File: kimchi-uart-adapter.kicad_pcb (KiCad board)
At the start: 2 copper layers, 50 x 20 mm, 29 parts, among them IC1 MIC5504-1.8YM5-TR, J1 TYPE-C-31-M-12, J2 Conn_01x02, J3 SM06B-SRSS-TB(LF)(SN), U1 TPD2E001DRSR, U2 FT230XS

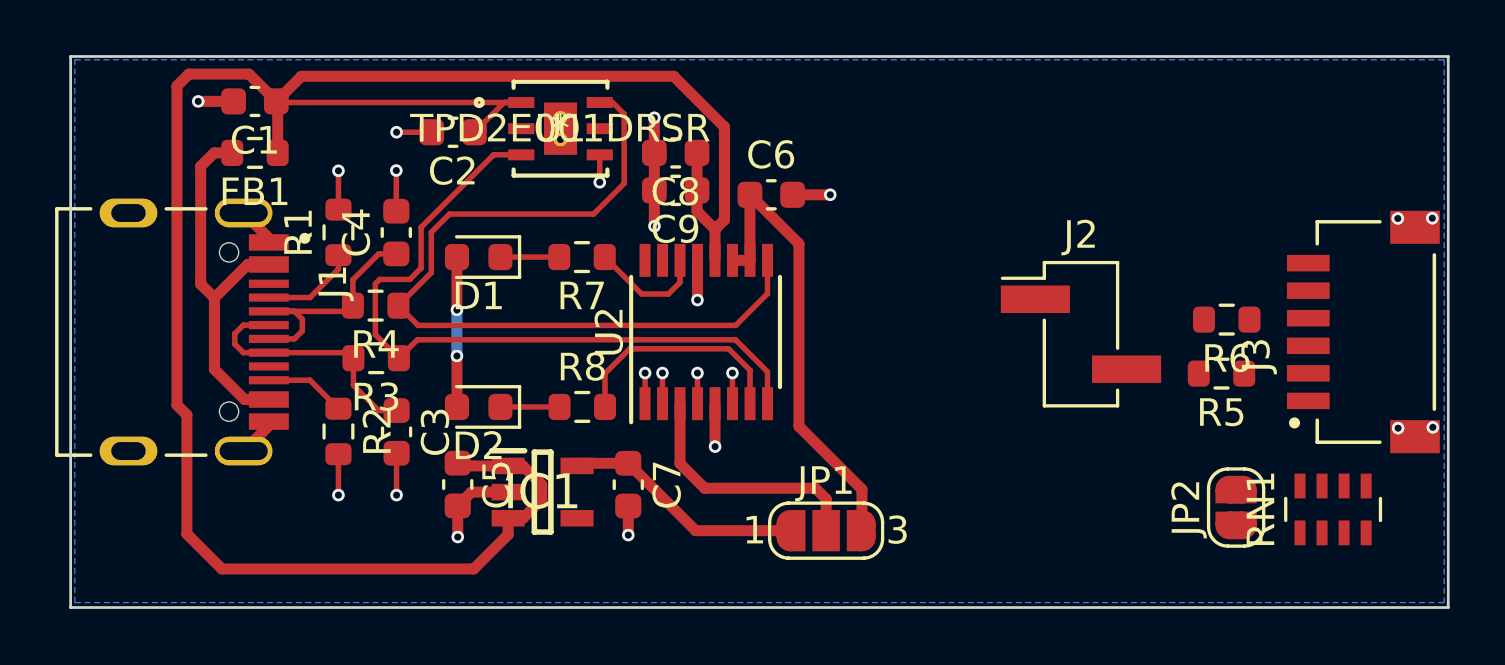
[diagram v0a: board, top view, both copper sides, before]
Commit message: Almost completed routing, waiting for fix to the resistor network issue. Also replaced model for TPD2E001 chip
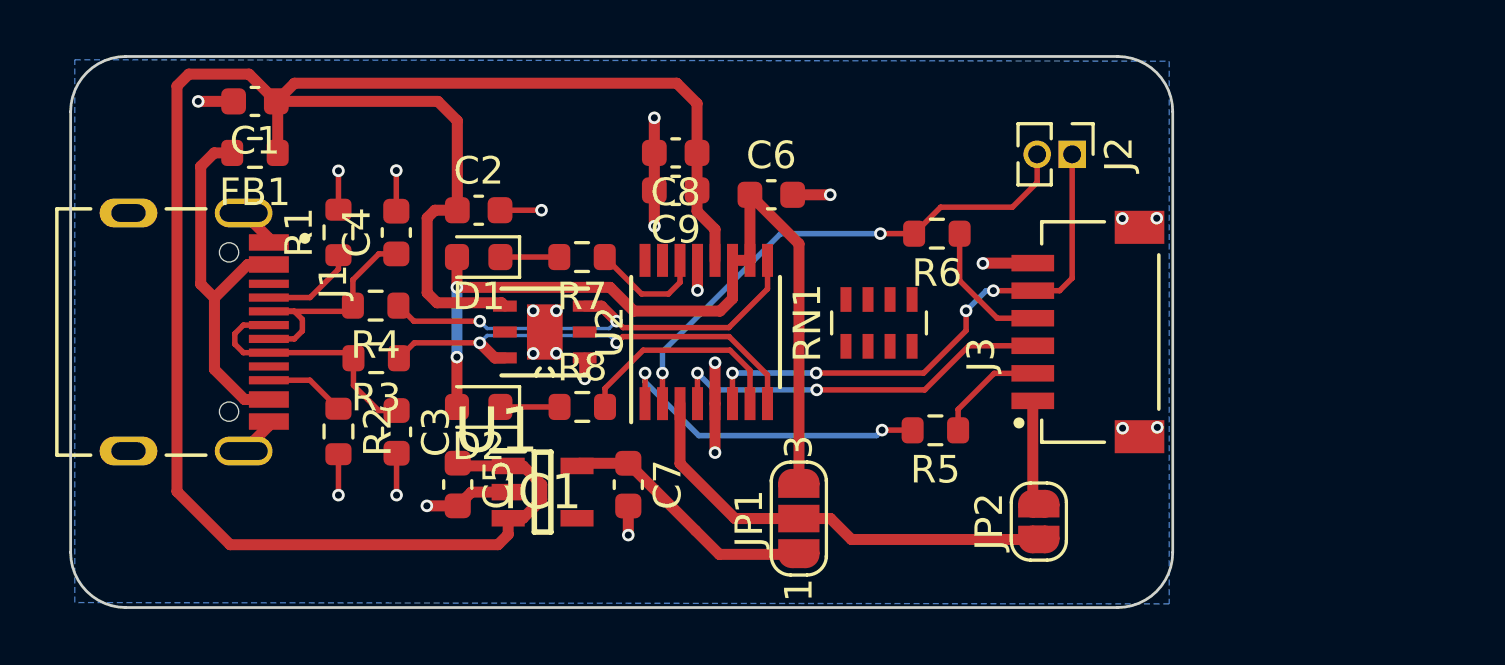
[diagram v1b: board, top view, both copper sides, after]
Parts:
- J2: footprint Connector_PinHeader_2.54mm:PinHeader_1x02_P2.54mm_Vertical_SMD_Pin1Left -> Connector_PinHeader_1.27mm:PinHeader_1x02_P1.27mm_Vertical
- U1: footprint footprints:TPD2E001DRSR -> footprints:SON95P315X315X80-7N
- moved RN1 17.8 mm to (163.2, 100.0)
- moved R6 11.0 mm to (165.3, 96.8)
- moved R5 10.6 mm to (165.2, 103.9)
- moved J3 10.0 mm to (168.8, 100.4)
- moved U1 7.40 mm to (151.1, 100.4), turned to 180 degrees
- moved JP2 7.18 mm to (169.0, 107.3)
- moved J2 6.54 mm to (170.2, 93.9), turned to 270 degrees
- moved C2 2.98 mm to (148.7, 96.0), turned to 0 degrees
- moved JP1 1.08 mm to (160.3, 107.2), turned to 90 degrees
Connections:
- D1 pad 2: +1V8 -> +3V3
- D2 pad 2: +1V8 -> +3V3
- U1 pad 1: VBUS -> GND
- U1 pad 3: /D1+ -> /D1-
- U1 pad 4: GND -> VBUS
- U1 pad 6: /D1- -> /D1+
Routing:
- net /CTS: track 1.11 -> 19.8 mm, vias 1 -> 4
- net /RTS: track 1.11 -> 19.0 mm, vias 1 -> 2
- net +3V3: track 16.9 -> 31.6 mm, vias 0 -> 2
- net /RX: track 1.11 -> 14.2 mm, vias 1 -> 2
- net /D1-: track 29.8 -> 17.5 mm, vias 0 -> 2
- net /TX: track 1.11 -> 12.0 mm, vias 1 -> 2
- net /D1+: track 26.4 -> 16.7 mm, vias 0 -> 2
- net /VCCIO: track 9.16 -> 16.3 mm
- net Net-(J3-Pad4): track 0.00 -> 4.92 mm
- net +1V8: track 14.2 -> 9.46 mm, vias 2 -> 0
- net Net-(J3-Pad2): track 0.00 -> 4.01 mm
- net /VCC_KIMCHI: track 0.00 -> 3.82 mm
- net GND: track 24.9 -> 28.0 mm, vias 18 -> 24
- net VBUS: track 77.7 -> 78.7 mm
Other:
- board size 50 x 20 mm -> 40 x 20 mm

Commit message: Completed routing
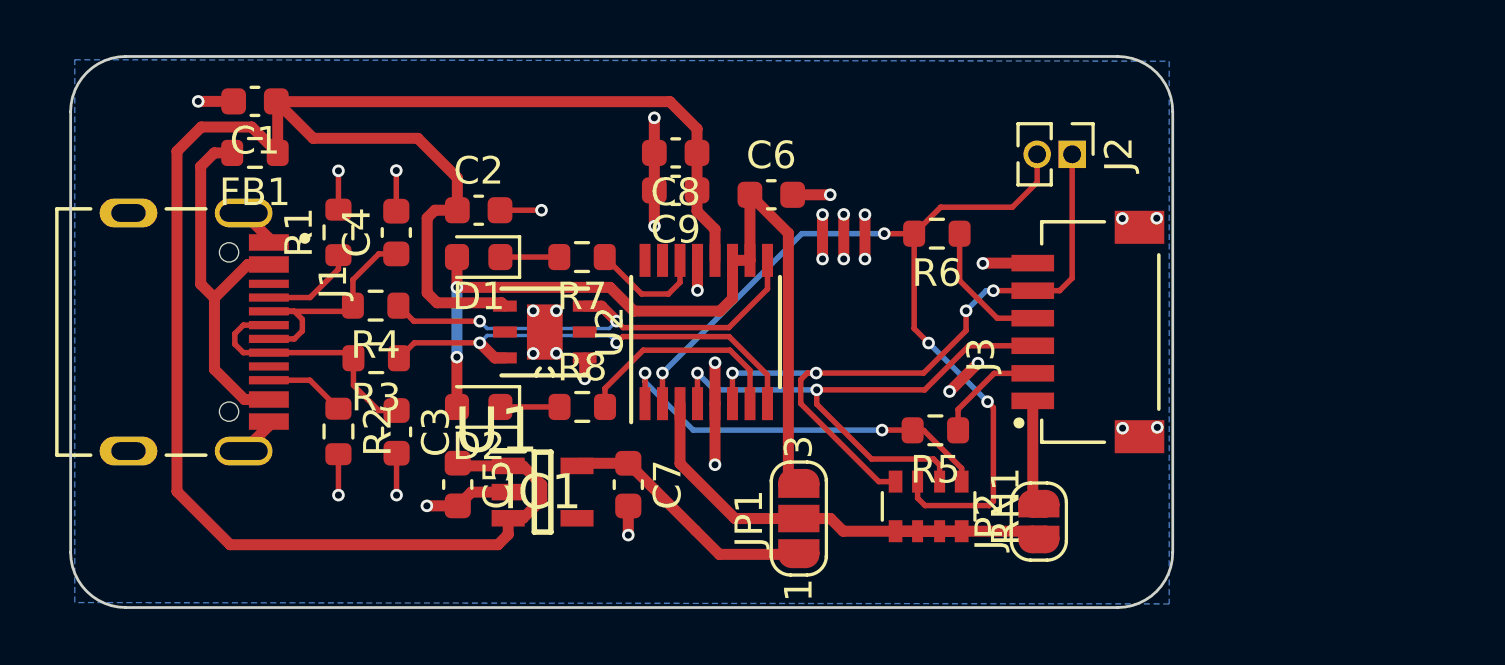
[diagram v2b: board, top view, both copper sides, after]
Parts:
- RN1: value R_Network04_US -> 10k; footprint Resistor_SMD:R_Array_Concave_4x0603 -> Resistor_SMD:R_Array_Convex_4x0603
- moved RN1 6.90 mm to (165.0, 106.7), turned to 270 degrees
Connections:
- RN1 pad 1: /VCCIO -> /TX
- RN1 pad 2: /TX -> /RX
- RN1 pad 3: /RX -> /RTS
- RN1 pad 4: /RTS -> /CTS
- RN1 pad 5: /CTS -> /VCCIO
- RN1 pad 6: (no net) -> /VCCIO
- RN1 pad 7: (no net) -> /VCCIO
- RN1 pad 8: (no net) -> /VCCIO
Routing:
- net /RTS: track 19.0 -> 33.0 mm, vias 2 -> 4
- net GND: track 28.0 -> 34.8 mm, vias 24 -> 32
- net /RX: track 14.2 -> 20.7 mm
- net /CTS: track 19.8 -> 25.9 mm
- net VBUS: track 78.7 -> 74.3 mm
- net /TX: track 12.0 -> 14.7 mm
- net /VCCIO: track 16.3 -> 18.7 mm
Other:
- rule trace_min: 0.0762 -> 0.127

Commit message: Completed routing of uart lid
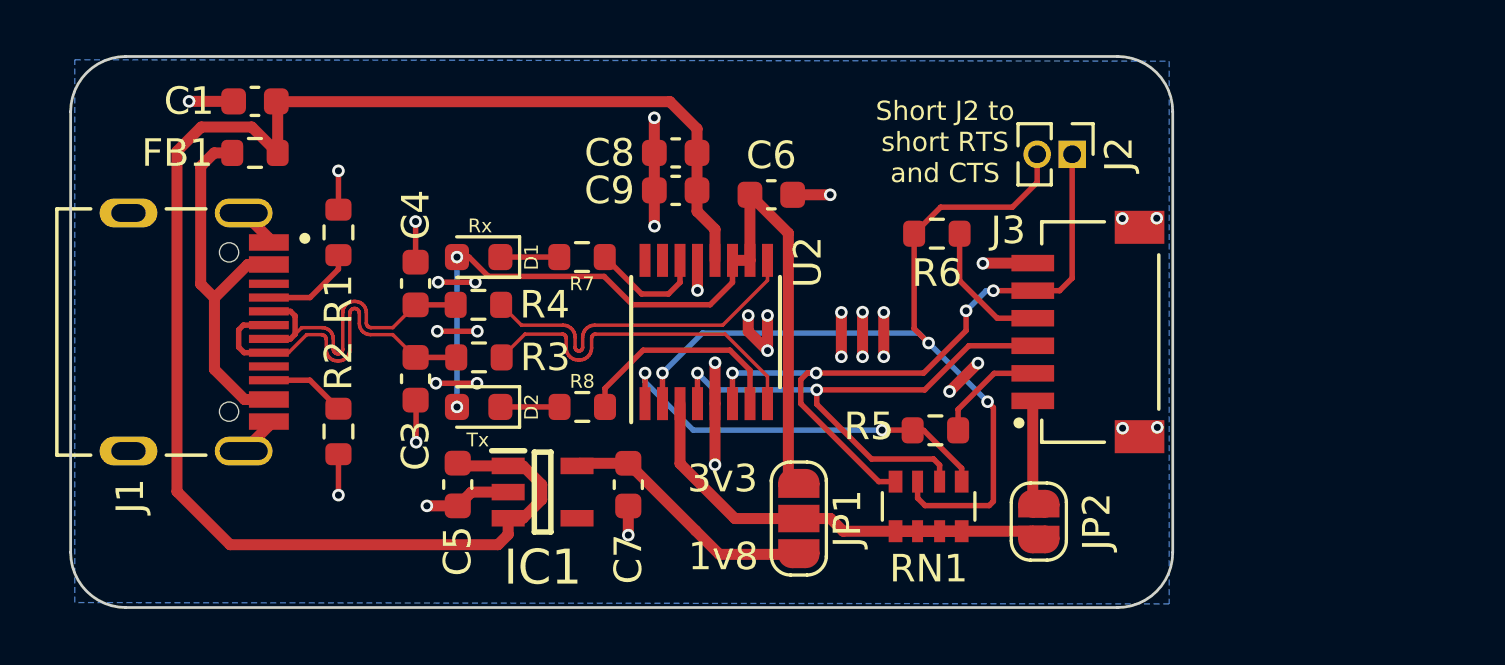
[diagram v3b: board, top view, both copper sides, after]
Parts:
- removed C2: 0.1uF, Capacitor_SMD:C_0603_1608Metric
- removed U1: TPD2E001DRSR, footprints:SON95P315X315X80-7N
- added REF**: OSHW-Logo2_7.3x6mm_SilkScreen, Symbol:OSHW-Logo2_7.3x6mm_SilkScreen, B.Cu at (138.9, 100.2)
- moved R4 3.73 mm to (148.7, 99.4)
- moved R3 3.73 mm to (148.7, 101.3)
- moved C3 2.05 mm to (146.4, 102.1)
- moved C4 1.98 mm to (146.4, 98.6)
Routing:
- net VBUS: track 74.3 -> 58.4 mm
- net GND: track 34.8 -> 40.0 mm, vias 32 -> 35
- net /D1-: track 17.5 -> 12.8 mm, vias 2 -> 0
- net /D+: track 9.19 -> 13.5 mm
- net /D-: track 9.13 -> 13.1 mm
- net /D1+: track 16.7 -> 13.0 mm, vias 2 -> 0
- net /RTS: track 33.0 -> 32.2 mm, vias 4 -> 3
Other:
- board text added: "1v8"
- board text added: "3v3"
- board text added: "Designed by Vedant Paranjape ve0x10.in"
- board text added: "Rx"
- board text added: "Short J2 to short RTS and CTS"
- board text added: "Tx"
- board text added: "USB to UART lid kimchi-micro"

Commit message: Updated silkscreen text
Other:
- board text added: "USB to UART adapter kimchi-micro"
- board text removed: "USB to UART lid kimchi-micro"

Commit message: Fixed changes requested during review, added gerbers and render images
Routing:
- net GND: track 40.0 -> 35.7 mm, vias 35 -> 29
- net +3V3: track 31.5 -> 31.0 mm, vias 2 -> 0
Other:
- rule pad_to_mask_clearance: 0.0508 -> 0
- rule trace_min: 0.127 -> 0.0762
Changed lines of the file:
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@@
-(kicad_pcb (version 20171130) (host pcbnew 5.1.10-88a1d61d58~88~ubuntu20.04.1)
+(kicad_pcb (version 20171130) (host pcbnew 5.1.10-88a1d61d58~90~ubuntu20.04.1)
   (general
     (thickness 1.6)
     (drawings 17)
-    (tracks 428)
+    (tracks 415)
     (zones 0)
     (modules 28)
@@
     (zone_clearance 0.508)
     (zone_45_only no)
-    (trace_min 0.127)
+    (trace_min 0.0762)
     (via_size 0.4572)
     (via_drill 0.254)
@@
     (pad_size 0.508 0.508)
     (pad_drill 0.254)
-    (pad_to_mask_clearance 0.0508)
-    (solder_mask_min_width 0.1016)
+    (pad_to_mask_clearance 0)
     (aux_axis_origin 0 0)
     (visible_elements FFFFFF7F)
@@
       (outputformat 1)
       (mirror false)
-      (drillshape 1)
+      (drillshape 0)
       (scaleselection 1)
-      (outputdirectory ""))
+      (outputdirectory "gerbers/"))
   )
   (net 0 "")
@@
     )
   )
+  (dimension 20 (width 0.15) (layer Dwgs.User)
+    (gr_text "20.000 mm" (at 178.78504 100.38 270) (layer Dwgs.User)
+      (effects (font (size 1 1) (thickness 0.15)))
+    )
+    (feature1 (pts (xy 171.85 110.38) (xy 178.071461 110.38)))
+    (feature2 (pts (xy 171.85 90.38) (xy 178.071461 90.38)))
+    (crossbar (pts (xy 177.48504 90.38) (xy 177.48504 110.38)))
+    (arrow1a (pts (xy 177.48504 110.38) (xy 176.898619 109.253496)))
+    (arrow1b (pts (xy 177.48504 110.38) (xy 178.071461 109.253496)))
+    (arrow2a (pts (xy 177.48504 90.38) (xy 176.898619 91.506504)))
+    (arrow2b (pts (xy 177.48504 90.38) (xy 178.071461 91.506504)))
+  )
+  (dimension 40 (width 0.15) (layer Dwgs.User)
+    (gr_text "40.000 mm" (at 153.85 114.680519) (layer Dwgs.User)
+      (effects (font (size 1 1) (thickness 0.15)))
+    )
+    (feature1 (pts (xy 173.85 108.38) (xy 173.85 113.96694)))
+    (feature2 (pts (xy 133.85 108.38) (xy 133.85 113.96694)))
+    (crossbar (pts (xy 133.85 113.380519) (xy 173.85 113.380519)))
+    (arrow1a (pts (xy 173.85 113.380519) (xy 172.723496 113.96694)))
+    (arrow1b (pts (xy 173.85 113.380519) (xy 172.723496 112.794098)))
+    (arrow2a (pts (xy 133.85 113.380519) (xy 134.976504 113.96694)))
+    (arrow2b (pts (xy 133.85 113.380519) (xy 134.976504 112.794098)))
+  )
+  (gr_text "USB to UART\nadapter\n kimchi-micro" (at 146.09318 100.05314 90) (layer B.SilkS)
+    (effects (font (size 1.5 1.5) (thickness 0.3)) (justify mirror))
+  )
   (gr_text "Designed by\nVedant Paranjape\nve0x10.in" (at 153.70556 100.5078 90) (layer B.SilkS)
     (effects (font (size 1.2 1.2) (thickness 0.3)) (justify mirror))
   )
-  (gr_text "USB to UART\nadapter\n kimchi-micro" (at 146.09318 100.05314 90) (layer B.SilkS)
-    (effects (font (size 1.5 1.5) (thickness 0.3)) (justify mirror))
-  )
   (gr_text "Short J2 to \nshort RTS \nand CTS" (at 165.58768 93.48724) (layer F.SilkS)
     (effects (font (size 0.7 0.7) (thickness 0.175)))
@@
   (gr_text Rx (at 148.71192 96.53016) (layer F.SilkS)
     (effects (font (size 0.5 0.5) (thickness 0.125)))
-  )
-  (dimension 20.010002 (width 0.15) (layer Dwgs.User)
-    (gr_text "20.010 mm" (at 180.894353 100.360452 -89.97136643) (layer Dwgs.User)
-      (effects (font (size 1 1) (thickness 0.15)))
-    )
-    (feature1 (pts (xy 171.79 90.36) (xy 180.175774 90.355809)))
-    (feature2 (pts (xy 171.8 110.37) (xy 180.185774 110.365809)))
-    (crossbar (pts (xy 179.599353 110.366102) (xy 179.589353 90.356102)))
-    (arrow1a (pts (xy 179.589353 90.356102) (xy 180.176337 91.482313)))
-    (arrow1b (pts (xy 179.589353 90.356102) (xy 179.003495 91.482899)))
-    (arrow2a (pts (xy 179.599353 110.366102) (xy 180.185211 109.239305)))
-    (arrow2b (pts (xy 179.599353 110.366102) (xy 179.012369 109.239891)))
-  )
-  (dimension 40.02008 (width 0.15) (layer Dwgs.User)
-    (gr_text "40.020 mm" (at 153.767127 114.489756 359.8854659) (layer Dwgs.User)
-      (effects (font (size 1 1) (thickness 0.15)))
-    )
-    (feature1 (pts (xy 173.79 108.09) (xy 173.778553 113.816178)))
-    (feature2 (pts (xy 133.77 108.01) (xy 133.758553 113.736178)))
-    (crossbar (pts (xy 133.759726 113.149759) (xy 173.779726 113.229759)))
-    (arrow1a (pts (xy 173.779726 113.229759) (xy 172.652052 113.813927)))
-    (arrow1b (pts (xy 173.779726 113.229759) (xy 172.654397 112.641088)))
-    (arrow2a (pts (xy 133.759726 113.149759) (xy 134.885055 113.73843)))
-    (arrow2b (pts (xy 133.759726 113.149759) (xy 134.8874 112.565591)))
   )
   (gr_line (start 173.85 108.38) (end 173.85 92.38) (layer Edge.Cuts) (width 0.1))
@@
   (segment (start 146.38782 104.37782) (end 146.39 104.38) (width 0.2) (layer F.Cu) (net 2))
   (segment (start 146.38782 102.85252) (end 146.38782 104.37782) (width 0.2) (layer F.Cu) (net 2))
-  (via (at 147.15744 100.35286) (size 0.4572) (drill 0.254) (layers F.Cu B.Cu) (net 2))
-  (via (at 148.61286 100.35286) (size 0.4572) (drill 0.254) (layers F.Cu B.Cu) (net 2))
-  (segment (start 147.15744 100.35286) (end 148.61286 100.35286) (width 0.2) (layer F.Cu) (net 2))
-  (via (at 147.10664 102.24008) (size 0.4572) (drill 0.254) (layers F.Cu B.Cu) (net 2))
-  (via (at 148.60016 102.24008) (size 0.4572) (drill 0.254) (layers F.Cu B.Cu) (net 2))
-  (segment (start 147.10664 102.24008) (end 148.60016 102.24008) (width 0.2) (layer F.Cu) (net 2))
-  (via (at 147.19046 98.57232) (size 0.4572) (drill 0.254) (layers F.Cu B.Cu) (net 2))
-  (via (at 148.5392 98.57486) (size 0.4572) (drill 0.254) (layers F.Cu B.Cu) (net 2))
-  (segment (start 148.53666 98.57232) (end 148.5392 98.57486) (width 0.2) (layer F.Cu) (net 2))
-  (segment (start 147.19046 98.57232) (end 148.53666 98.57232) (width 0.2) (layer F.Cu) (net 2))
   (via (at 158.44266 99.7839) (size 0.4572) (drill 0.254) (layers F.Cu B.Cu) (net 2))
   (via (at 159.1437 99.78136) (size 0.4572) (drill 0.254) (layers F.Cu B.Cu) (net 2))
@@
   (segment (start 158.505 97.7775) (end 158.5075 97.78) (width 0.4) (layer F.Cu) (net 5))
   (segment (start 158.505 95.4) (end 158.505 97.7775) (width 0.4) (layer F.Cu) (net 5))
-  (segment (start 147.87 103.0975) (end 147.8725 103.1) (width 0.4) (layer F.Cu) (net 5))
   (segment (start 159.9 105.47) (end 160.28 105.85) (width 0.4) (layer F.Cu) (net 5))
   (segment (start 159.9 96.795) (end 159.9 105.47) (width 0.4) (layer F.Cu) (net 5))
   (segment (start 158.505 95.4) (end 159.9 96.795) (width 0.4) (layer F.Cu) (net 5))
-  (segment (start 147.87 97.6625) (end 147.8725 97.66) (width 0.4) (layer F.Cu) (net 5))
   (segment (start 147.8725 97.66) (end 147.8725 97.66) (width 0.4) (layer F.Cu) (net 5))
-  (via (at 147.8725 97.66) (size 0.4572) (drill 0.254) (layers F.Cu B.Cu) (net 5))
   (segment (start 147.8725 103.1) (end 147.8725 103.1) (width 0.4) (layer F.Cu) (net 5))
-  (via (at 147.8725 103.1) (size 0.4572) (drill 0.254) (layers F.Cu B.Cu) (net 5))
-  (segment (start 147.8725 97.66) (end 147.8725 103.1) (width 0.2) (layer B.Cu) (net 5))
-  (segment (start 149.01201 98.36201) (end 148.31 97.66) (width 0.2) (layer F.Cu) (net 5))
-  (segment (start 153.21334 98.36201) (end 149.01201 98.36201) (width 0.2) (layer F.Cu) (net 5))
-  (segment (start 148.31 97.66) (end 147.8725 97.66) (width 0.2) (layer F.Cu) (net 5))
-  (segment (start 154.241529 99.390199) (end 153.21334 98.36201) (width 0.2) (layer F.Cu) (net 5))
+  (segment (start 147.87 103.0975) (end 147.8725 103.1) (width 0.4) (layer F.Cu) (net 5))
+  (segment (start 157.062301 99.390199) (end 154.241529 99.390199) (width 0.2) (layer F.Cu) (net 5))
+  (segment (start 157.8725 97.78) (end 157.8725 98.58) (width 0.2) (layer F.Cu) (net 5))
   (segment (start 157.8725 98.58) (end 157.062301 99.390199) (width 0.2) (layer F.Cu) (net 5))
-  (segment (start 157.8725 97.78) (end 157.8725 98.58) (width 0.2) (layer F.Cu) (net 5))
-  (segment (start 157.062301 99.390199) (end 154.241529 99.390199) (width 0.2) (layer F.Cu) (net 5))
+  (segment (start 148.68398 102.28852) (end 147.8725 103.1) (width 0.2) (layer F.Cu) (net 5))
+  (segment (start 148.68398 98.47148) (end 148.68398 102.28852) (width 0.2) (layer F.Cu) (net 5))
+  (segment (start 147.8725 97.66) (end 148.68398 98.47148) (width 0.2) (layer F.Cu) (net 5))
+  (segment (start 153.32281 98.47148) (end 154.241529 99.390199) (width 0.2) (layer F.Cu) (net 5))
+  (segment (start 148.68398 98.47148) (end 153.32281 98.47148) (width 0.2) (layer F.Cu) (net 5))
   (segment (start 152.325 105.145) (end 152.23 105.24) (width 0.4) (layer F.Cu) (net 6))
   (segment (start 154.09 105.145) (end 152.325 105.145) (width 0.4) (layer F.Cu) (net 6))
